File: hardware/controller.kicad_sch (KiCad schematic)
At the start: 55 parts, among them J1 HC-TYPE-C-16P-CB1.6, J2 AXK6F20347YG, J3 AFA01-S08FCA-00, SW1 SSSS811101, U1 ESP32-C6-WROOM-1-N8, U2 BQ24074RGTR, U3 TLA2518IRTER, U6 TPS62142RGTR

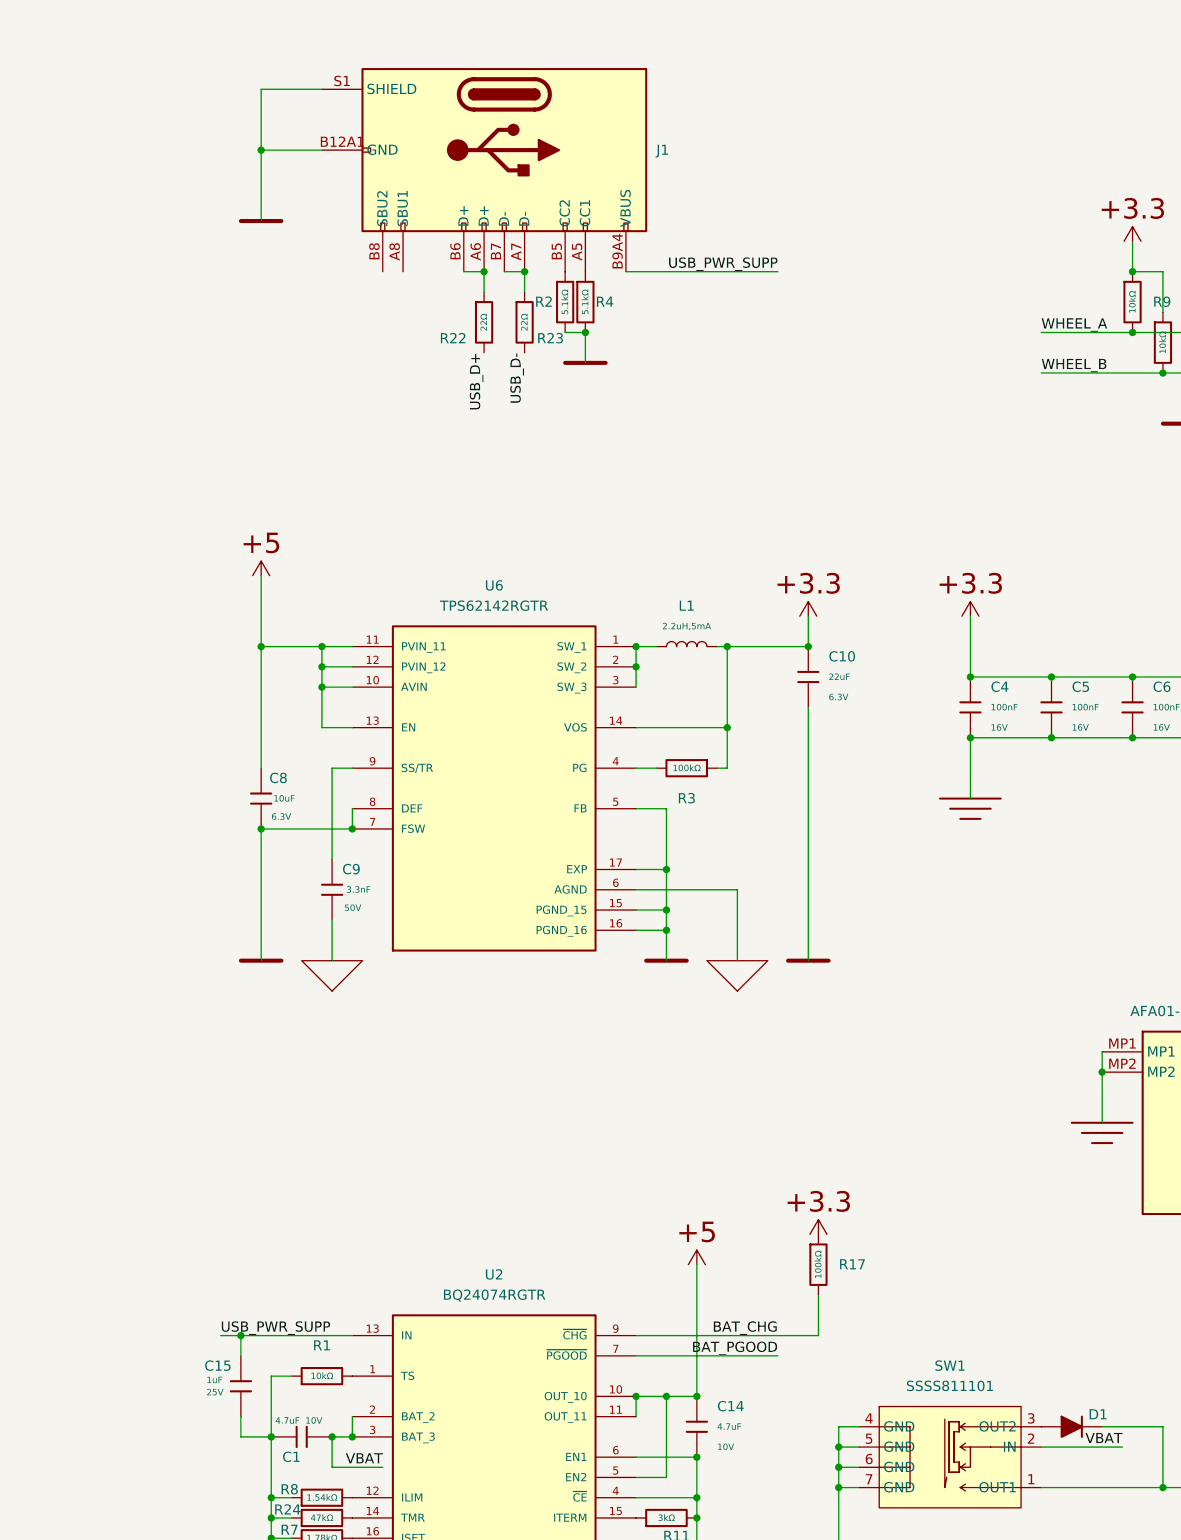
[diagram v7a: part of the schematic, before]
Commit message: :sparkles: esd protection for type-c
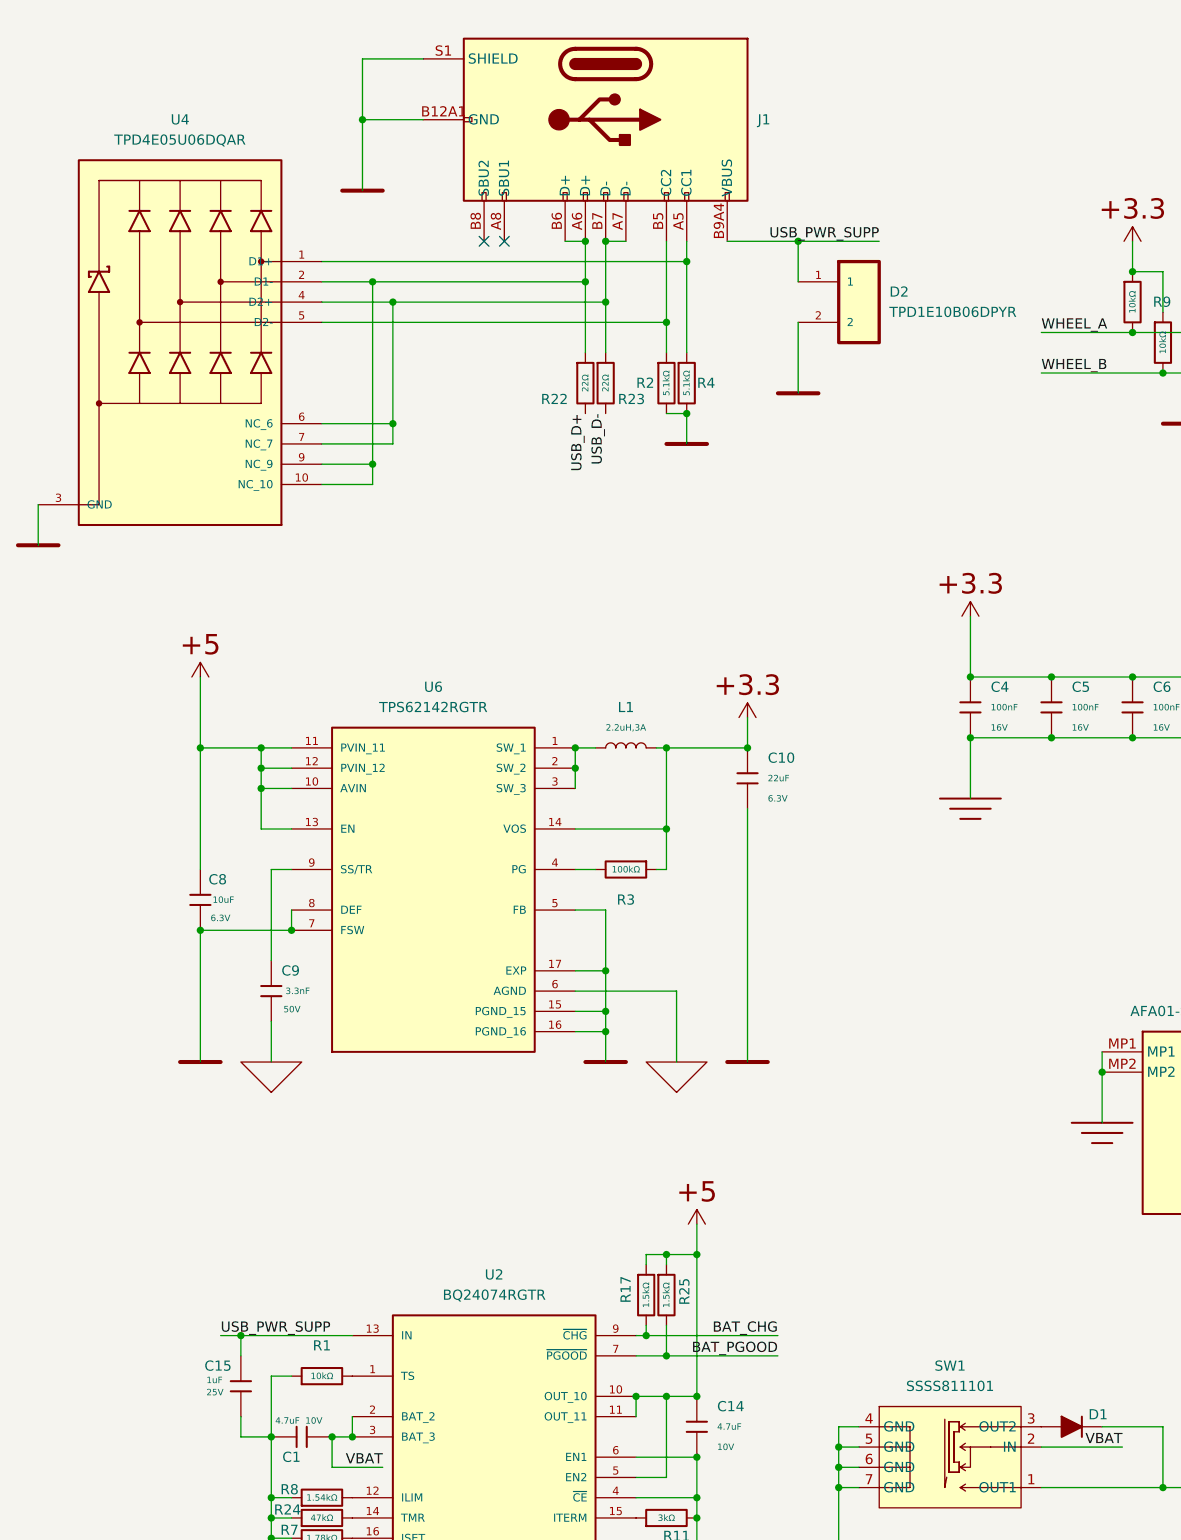
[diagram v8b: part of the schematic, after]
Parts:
- removed R17: 100kΩ, KeysDock:R_0402, symbol components:0402,100kΩ
- added D2: TPD1E10B06DPYR, KeysDock:DIO_TPD1E05U06DPYR, symbol components:TPD1E10B06DPYR
- added R17, R25: 1.5kΩ, KeysDock:R_0402, symbol components:0402,1.5kΩ
- added U4: TPD4E05U06DQAR, KeysDock:IC_TPD4E05U06DQAR, symbol components:TPD4E05U06DQAR
- L1: value 2.2uH,5mA -> 2.2uH,3A
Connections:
- net BAT_CHG: now also R17.2
- net BAT_PGOOD: now also R25.2
- net P,+5: now also R17.1, R25.1
- net USB_PWR_SUPP: now also D2.1
- net at J1.A5 (CC1), R4.1: now also U4.1 (D1+)
- net at J1.A6 (D+), J1.B6 (D+), R22.1: now also U4.10 (NC_10), U4.2 (D1-), U4.9 (NC_9)
- net at J1.A7 (D-), J1.B7 (D-), R23.1: now also U4.4 (D2+), U4.6 (NC_6), U4.7 (NC_7)
- net at J1.B5 (CC2), R2.1: now also U4.5 (D2-)
- net P,E renamed GND
- net GND: now also D2.2, U4.3 (GND), U4.8 (GND)
- no-connect marks 3 -> 5
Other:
- moved on the sheet: C10, C8, C9, J1, L1, R2, R22, R23, R3, R4, U6
